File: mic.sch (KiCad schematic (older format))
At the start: 8 parts, among them J6 JACK_TRS_5PINS

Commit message: Fix labels and lay resistors flat.
Left inputs to the line driver were backwards, because the datasheet had
an error. I think I "fixed"it before to match the datasheet.

I also decided to lay the resistors flat. They don't take up that much
room flat, and they will be easier to make pretty on the board, and more
stable with all the vibration.

Also updated the BOM and netlist.
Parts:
- R4, R5: footprint Resistors_THT:R_Axial_DIN0204_L3.6mm_D1.6mm_P1.90mm_Vertical -> Resistors_THT:R_Axial_DIN0204_L3.6mm_D1.6mm_P5.08mm_Horizontal
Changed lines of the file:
@@
 F 0 "R4" V 5830 4000 50  0000 C CNN
 F 1 "2k2" V 5750 4000 50  0000 C CNN
-F 2 "Resistors_THT:R_Axial_DIN0204_L3.6mm_D1.6mm_P1.90mm_Vertical" V 5680 4000 50  0001 C CNN
+F 2 "Resistors_THT:R_Axial_DIN0204_L3.6mm_D1.6mm_P5.08mm_Horizontal" V 5680 4000 50  0001 C CNN
 F 3 "https://www.seielect.com/Catalog/SEI-RNF_RNMF.pdf" H 5750 4000 50  0001 C CNN
 	1    5750 4000
@@
 F 0 "R5" V 6030 3950 50  0000 C CNN
 F 1 "2k2" V 5950 3950 50  0000 C CNN
-F 2 "Resistors_THT:R_Axial_DIN0204_L3.6mm_D1.6mm_P1.90mm_Vertical" V 5880 3950 50  0001 C CNN
+F 2 "Resistors_THT:R_Axial_DIN0204_L3.6mm_D1.6mm_P5.08mm_Horizontal" V 5880 3950 50  0001 C CNN
 F 3 "https://www.seielect.com/Catalog/SEI-RNF_RNMF.pdf" H 5950 3950 50  0001 C CNN
 	1    5950 3950

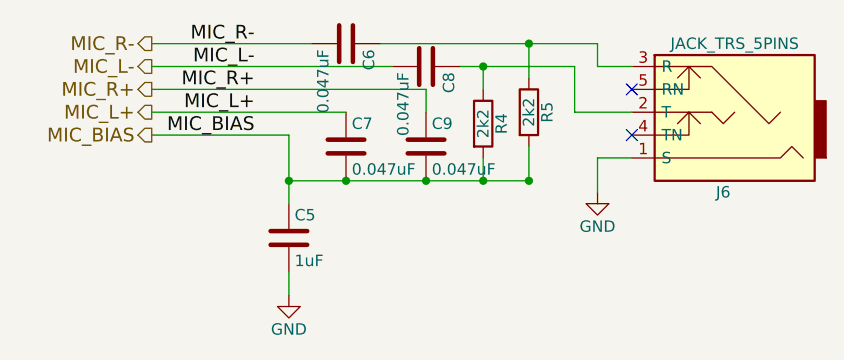
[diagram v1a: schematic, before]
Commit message: Add a line in module and use a smaller jack.
Lots of changes:
Added a line in. This requires another audio switch, so that's added to
the audio switch module.
Also, since I'm using two jacks, I chose a smaller jack module. This
needed a new footprint, and a new 3d model. The footprint is trickier,
since it really needed slots, which OSH won't guarantee. I've given it a
unique footprint to try to optimize the pad size around the edges of the
pins.
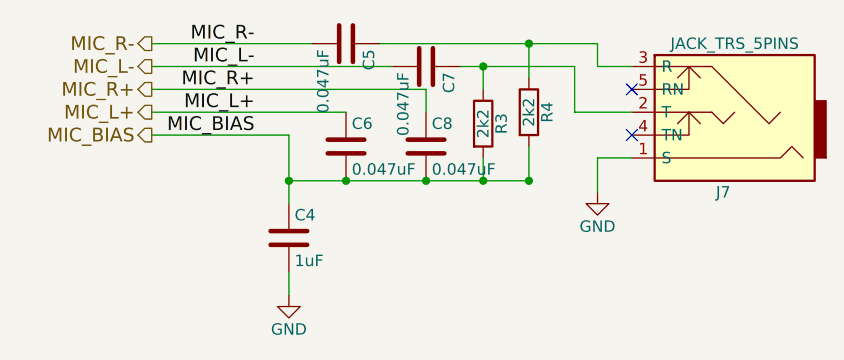
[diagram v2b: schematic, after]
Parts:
- J7: renamed from J6; footprint blubaru:SJ1-3523NG -> blubaru:sj1-353xng
- renumbered C5 to C4, C6 to C5, C7 to C6, C8 to C7, C9 to C8, R4 to R3, R5 to R4
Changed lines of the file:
@@
 $Descr USLetter 11000 8500
 encoding utf-8
-Sheet 7 8
+Sheet 7 10
 Title "Blubaru"
 Date "2017-02-28"
@@
 MIC_BIAS
 $Comp
-L C C8
+L C C7
 U 1 1 589D21D3
 P 5500 3750
-F 0 "C8" H 5525 3850 50  0000 L CNN
+F 0 "C7" H 5525 3850 50  0000 L CNN
 F 1 "0.047uF" H 5525 3650 50  0000 L CNN
 F 2 "blubaru:C_Disc_D4.0mm_W2.6mm_P2.50mm" H 5538 3600 50  0001 C CNN
@@
 $EndComp
 $Comp
-L C C7
+L C C6
 U 1 1 589D223D
 P 5150 4100
-F 0 "C7" H 5175 4200 50  0000 L CNN
+F 0 "C6" H 5175 4200 50  0000 L CNN
 F 1 "0.047uF" H 5175 4000 50  0000 L CNN
 F 2 "blubaru:C_Disc_D4.0mm_W2.6mm_P2.50mm" H 5188 3950 50  0001 C CNN
@@
 $EndComp
 $Comp
-L C C9
+L C C8
 U 1 1 589D230D
 P 5500 4100
-F 0 "C9" H 5525 4200 50  0000 L CNN
+F 0 "C8" H 5525 4200 50  0000 L CNN
 F 1 "0.047uF" H 5525 4000 50  0000 L CNN
 F 2 "blubaru:C_Disc_D4.0mm_W2.6mm_P2.50mm" H 5538 3950 50  0001 C CNN
@@
 $EndComp
 $Comp
-L C C5
+L C C4
 U 1 1 589D2382
 P 4900 4500
-F 0 "C5" H 4925 4600 50  0000 L CNN
+F 0 "C4" H 4925 4600 50  0000 L CNN
 F 1 "1uF" H 4925 4400 50  0000 L CNN
 F 2 "blubaru:C_Disc_D5.0mm_W3.2mm_P2.50mm" H 4938 4350 50  0001 C CNN
@@
 $EndComp
 $Comp
-L C C6
+L C C5
 U 1 1 589D23FA
 P 5150 3650
-F 0 "C6" H 5175 3750 50  0000 L CNN
+F 0 "C5" H 5175 3750 50  0000 L CNN
 F 1 "0.047uF" H 5175 3550 50  0000 L CNN
 F 2 "blubaru:C_Disc_D4.0mm_W2.6mm_P2.50mm" H 5188 3500 50  0001 C CNN
@@
 $EndComp
 $Comp
-L R R4
+L R R3
 U 1 1 589D2492
 P 5750 4000
-F 0 "R4" V 5830 4000 50  0000 C CNN
+F 0 "R3" V 5830 4000 50  0000 C CNN
 F 1 "2k2" V 5750 4000 50  0000 C CNN
 F 2 "Resistors_THT:R_Axial_DIN0204_L3.6mm_D1.6mm_P5.08mm_Horizontal" V 5680 4000 50  0001 C CNN
@@
 $EndComp
 $Comp
-L R R5
+L R R4
 U 1 1 589D2525
 P 5950 3950
-F 0 "R5" V 6030 3950 50  0000 C CNN
+F 0 "R4" V 6030 3950 50  0000 C CNN
 F 1 "2k2" V 5950 3950 50  0000 C CNN
 F 2 "Resistors_THT:R_Axial_DIN0204_L3.6mm_D1.6mm_P5.08mm_Horizontal" V 5880 3950 50  0001 C CNN
@@
 MIC_BIAS
 $Comp
-L JACK_TRS_5PINS J6
+L JACK_TRS_5PINS J7
 U 1 1 58BF91C1
 P 6800 3950
-F 0 "J6" H 6800 4300 50  0000 C CNN
+F 0 "J7" H 6800 4300 50  0000 C CNN
 F 1 "JACK_TRS_5PINS" H 6750 3650 50  0000 C CNN
-F 2 "blubaru:SJ1-3523NG" H 6900 3800 50  0001 C CNN
+F 2 "blubaru:sj1-353xng" H 6900 3800 50  0001 C CNN
 F 3 "http://www.cui.com/product/resource/sj1-352xng-series.pdf" H 6900 3800 50  0001 C CNN
 	1    6800 3950
